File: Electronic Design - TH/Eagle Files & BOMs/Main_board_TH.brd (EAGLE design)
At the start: 98 x 137 mm, 43 parts, among them M1 ARDUINO-NANO-3.0, Q1 IRF9520, Q2 IRF9520

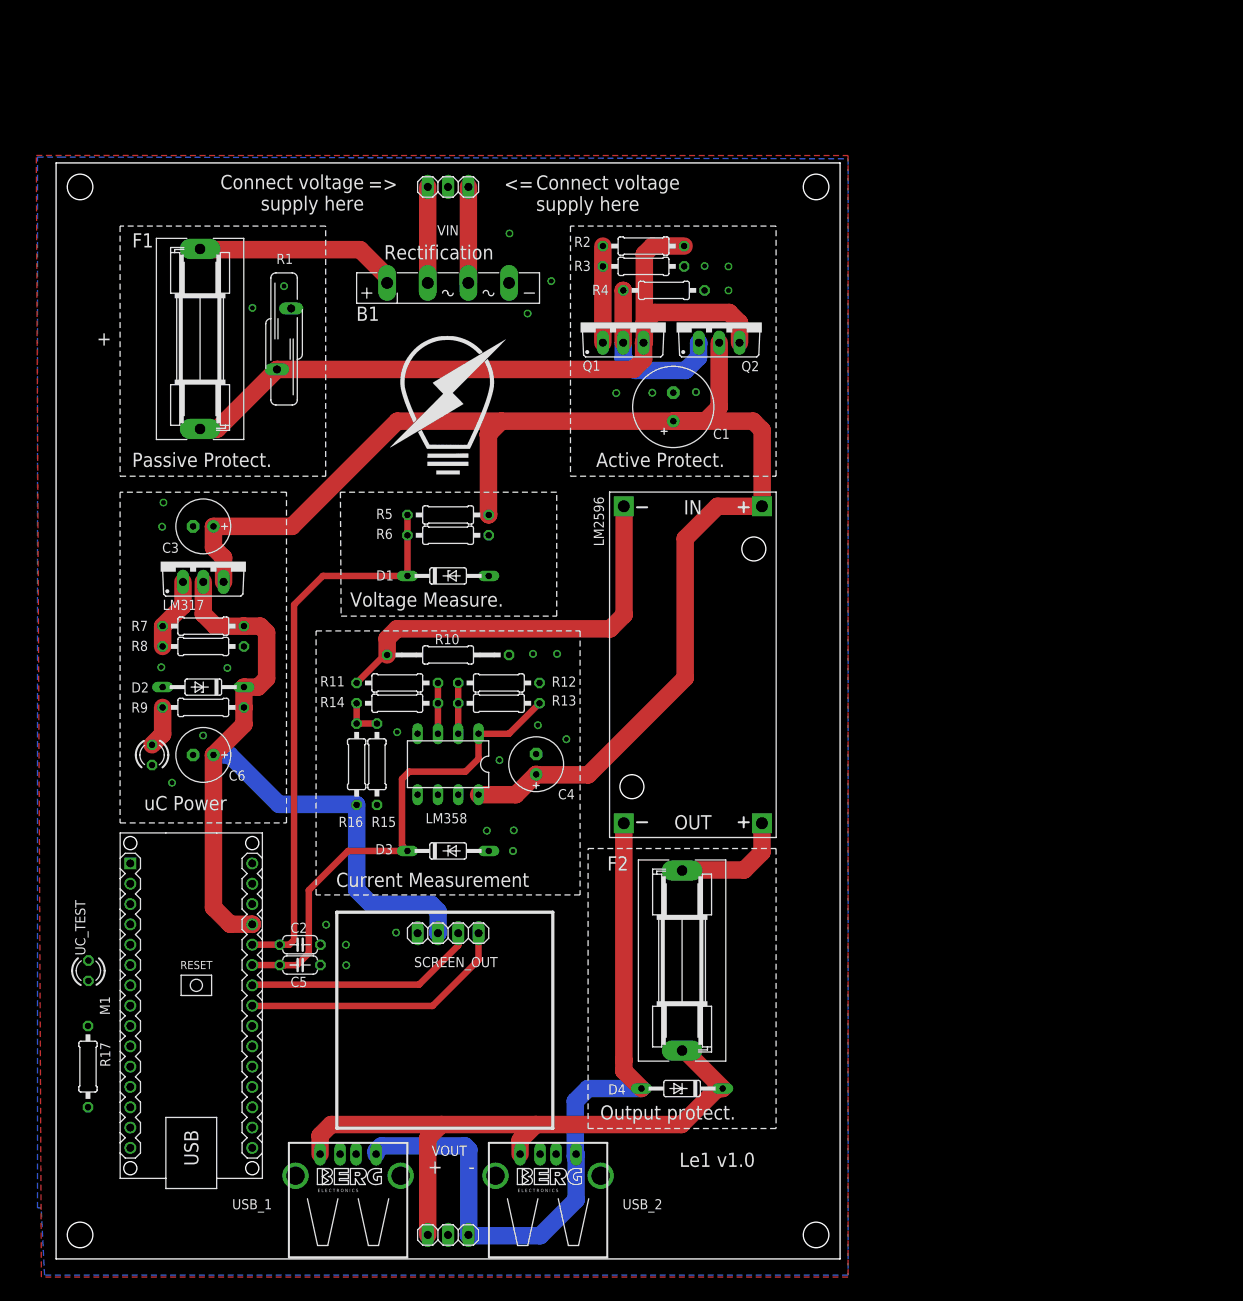
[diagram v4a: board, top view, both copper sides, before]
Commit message: adding in test points and jumpers
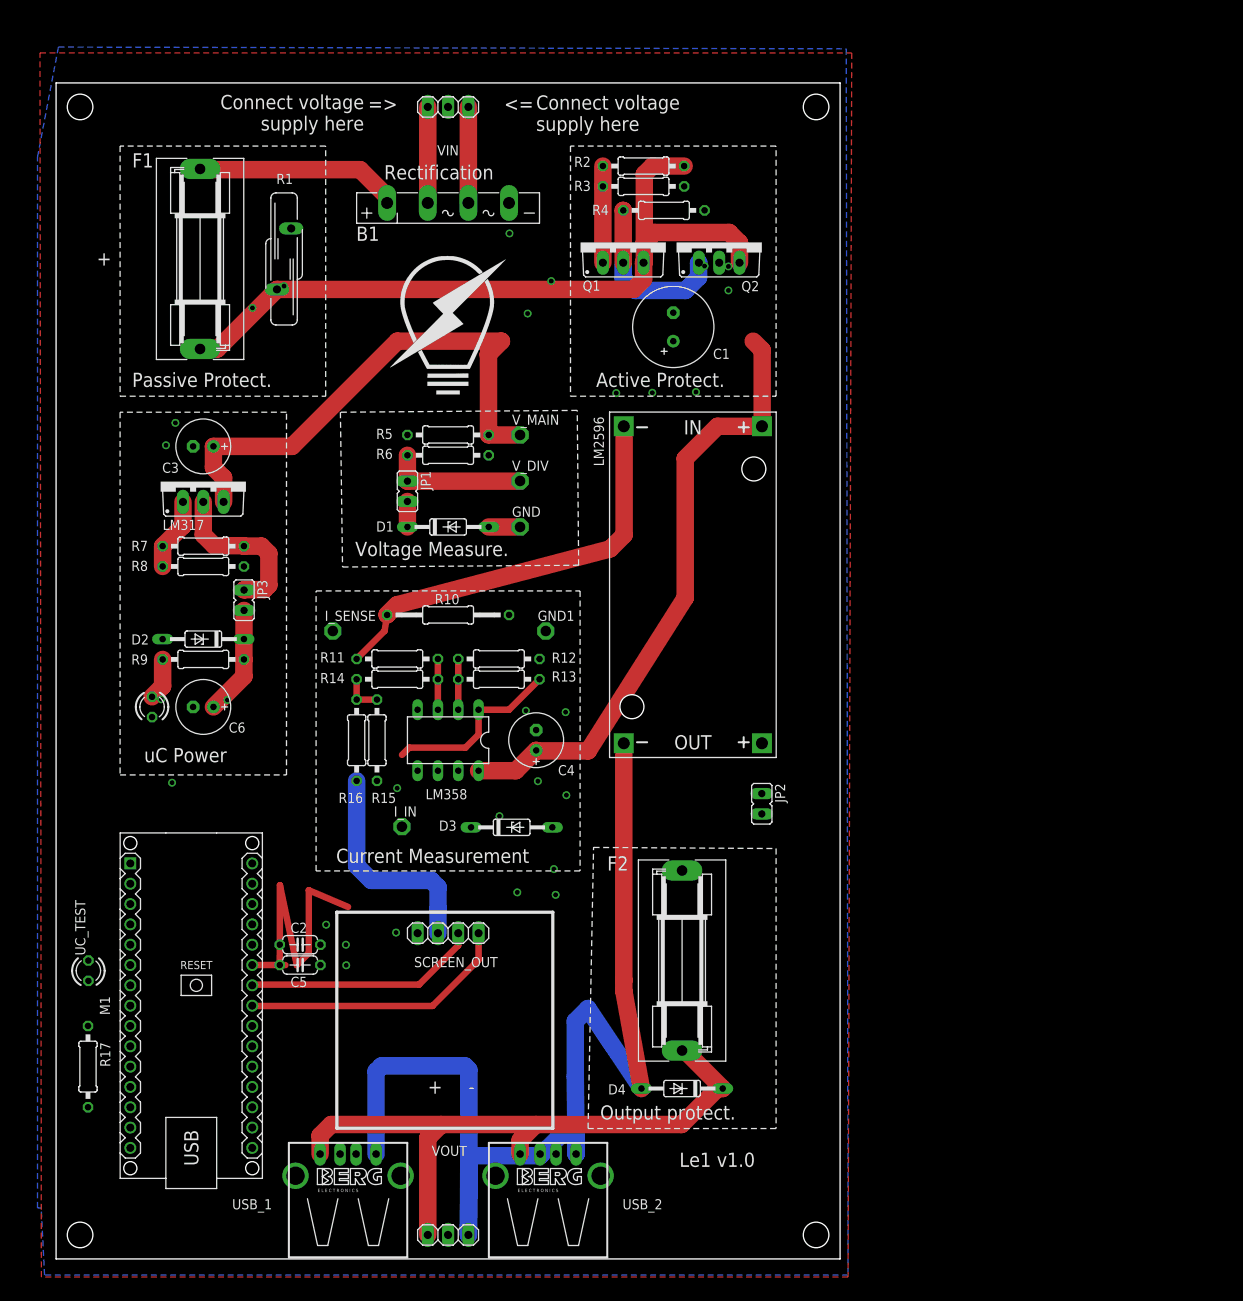
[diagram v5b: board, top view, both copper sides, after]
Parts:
- added GND, GND1, I_IN, I_SENSE, V_DIV, V_MAIN: TPPAD1-13, testpad:P1-13
- added JP1, JP2, JP3: (no value), jumper:JP1
- moved R2 10.0 mm to (73.4, 136.6)
- moved B1 10.0 mm to (49.0, 132.0)
- moved C1 10.0 mm to (77.2, 116.5)
- moved C3 10.0 mm to (18.4, 101.6)
- moved F1 10.0 mm to (18.0, 125.0)
- moved LM2596 10.0 mm to (79.6, 84.3)
- moved LM317 10.0 mm to (18.4, 97.2)
- moved Q1 10.0 mm to (70.9, 127.1)
- moved Q2 10.0 mm to (82.9, 127.1)
- moved R1 10.0 mm to (28.5, 125.0)
- moved R3 10.0 mm to (73.4, 134.1)
- moved R4 10.0 mm to (76.0, 131.1)
- moved R5 10.0 mm to (49.0, 103.0)
- moved R6 10.0 mm to (49.0, 100.5)
- moved R7 10.0 mm to (18.4, 89.1)
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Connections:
- removed net VOUT_PREFUSE: F2.1, LM2596.OUT+
- new net N$15: JP2.1, LM2596.OUT+
- new net N$16: F2.1, JP2.2
- new net N$17: JP1.1, R5.1, R6.2, V_DIV.TP
- new net N$18: JP3.1, LM317.2, R7.2
- net +5V: now also JP3.2; no longer LM317.2, R7.2
- net GND: now also GND.TP, GND1.TP
- net I_IN: now also I_IN.TP
- net N$4: now also I_SENSE.TP
- net VIN_PROTECTED: now also V_MAIN.TP
- net V_IN: now also JP1.2; no longer R5.1, R6.2
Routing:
- net V_IN: track 70.7 -> 3.18 mm
- net +5V: track 101.9 -> 41.3 mm
- net N$10: track 94.4 -> 146.7 mm
- net VIN_PROTECTED: track 179.1 -> 142.5 mm
- net N$18: track 0.00 -> 20.6 mm
- net N$17: track 0.00 -> 17.3 mm
- net VOUT_PREFUSE: track 16.9 -> 0.00 mm
- net GND: track 0.00 -> 3.92 mm, vias 30 -> 29
- net N$4: track 51.7 -> 52.4 mm
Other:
- board size 98 x 137 mm -> 98 x 147 mm

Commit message: putting all components into the right places before rounting
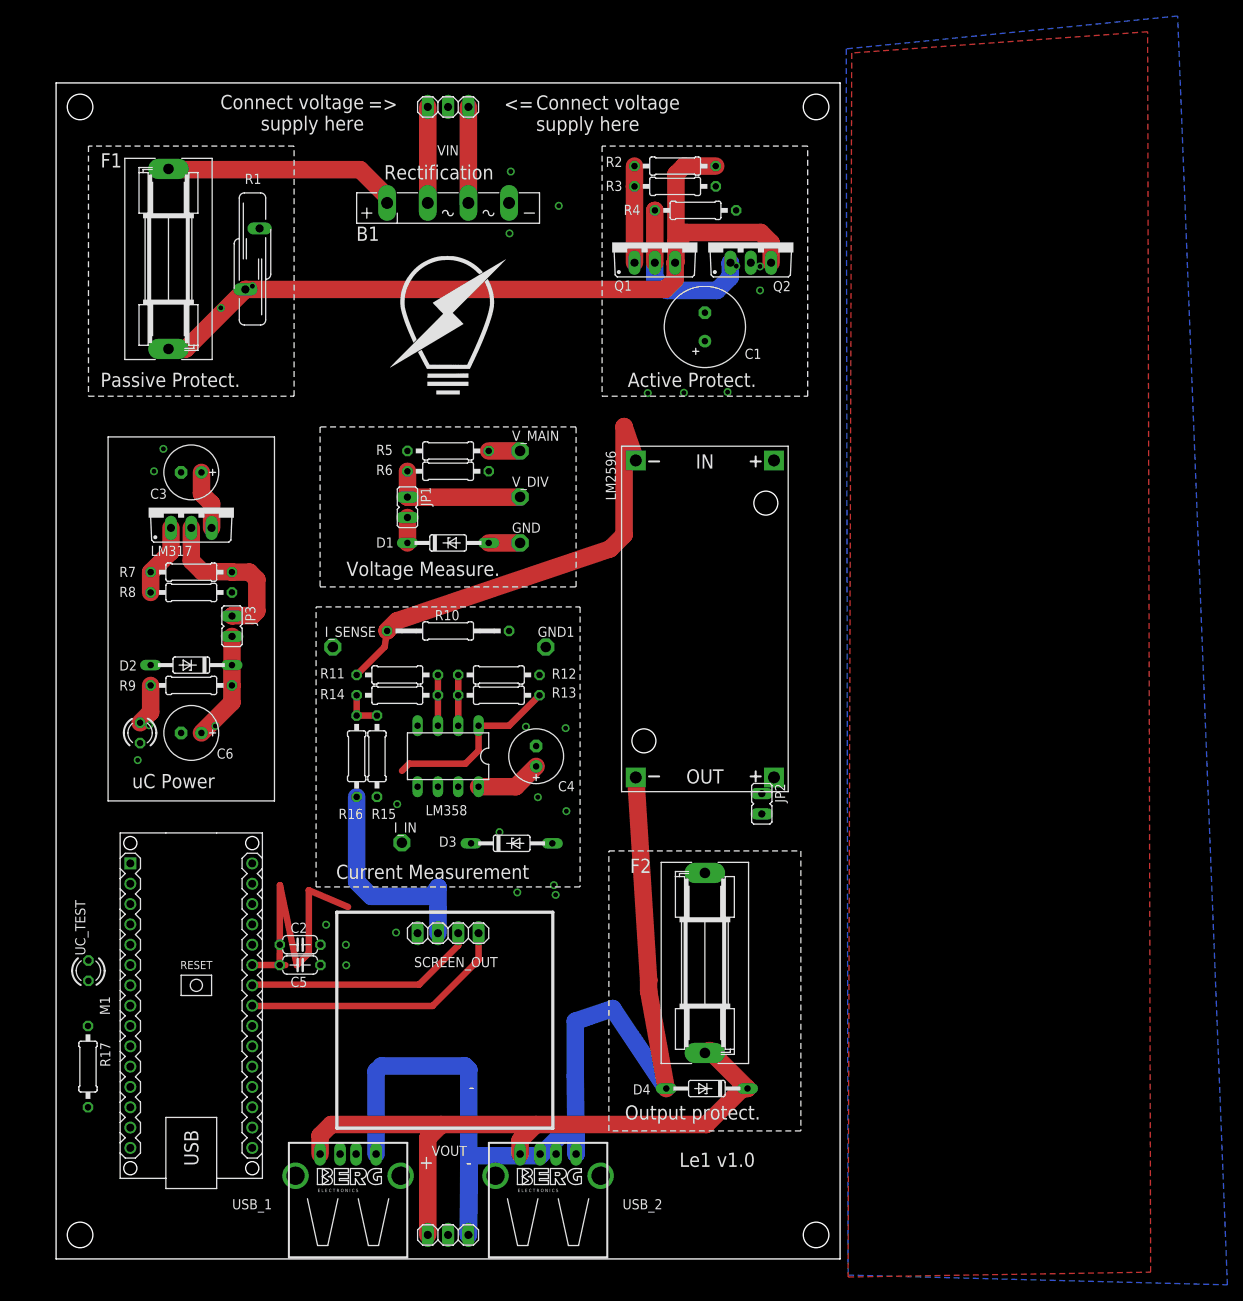
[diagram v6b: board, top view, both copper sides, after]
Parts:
- moved LM2596 4.53 mm to (81.1, 80.0)
- moved Q1 3.95 mm to (74.8, 127.1)
- moved Q2 3.95 mm to (86.8, 127.1)
- moved R4 3.95 mm to (79.9, 131.1)
- moved F1 3.95 mm to (14.1, 125.0)
- moved R1 3.95 mm to (24.6, 125.0)
- moved C1 3.95 mm to (81.1, 116.5)
- moved R2 3.95 mm to (77.4, 136.6)
- moved R3 3.95 mm to (77.4, 134.1)
- moved C3 3.58 mm to (16.9, 98.3)
- moved C6 3.58 mm to (16.9, 65.8)
- moved D2 3.58 mm to (16.9, 74.2)
- moved JP3 3.58 mm to (22.0, 79.1)
- moved LM317 3.58 mm to (16.9, 93.9)
- moved R7 3.58 mm to (16.9, 85.8)
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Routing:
- net VIN_PROTECTED: track 142.5 -> 19.6 mm
- net VIN_UNPROTECTED: track 93.1 -> 101.0 mm
- net N$4: track 52.4 -> 57.4 mm
- net N$1: track 26.4 -> 30.3 mm
- net VOUT_FINAL: track 81.1 -> 84.6 mm
- net N$10: track 146.7 -> 145.2 mm

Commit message: adding another jumper after current sensing and more routing done
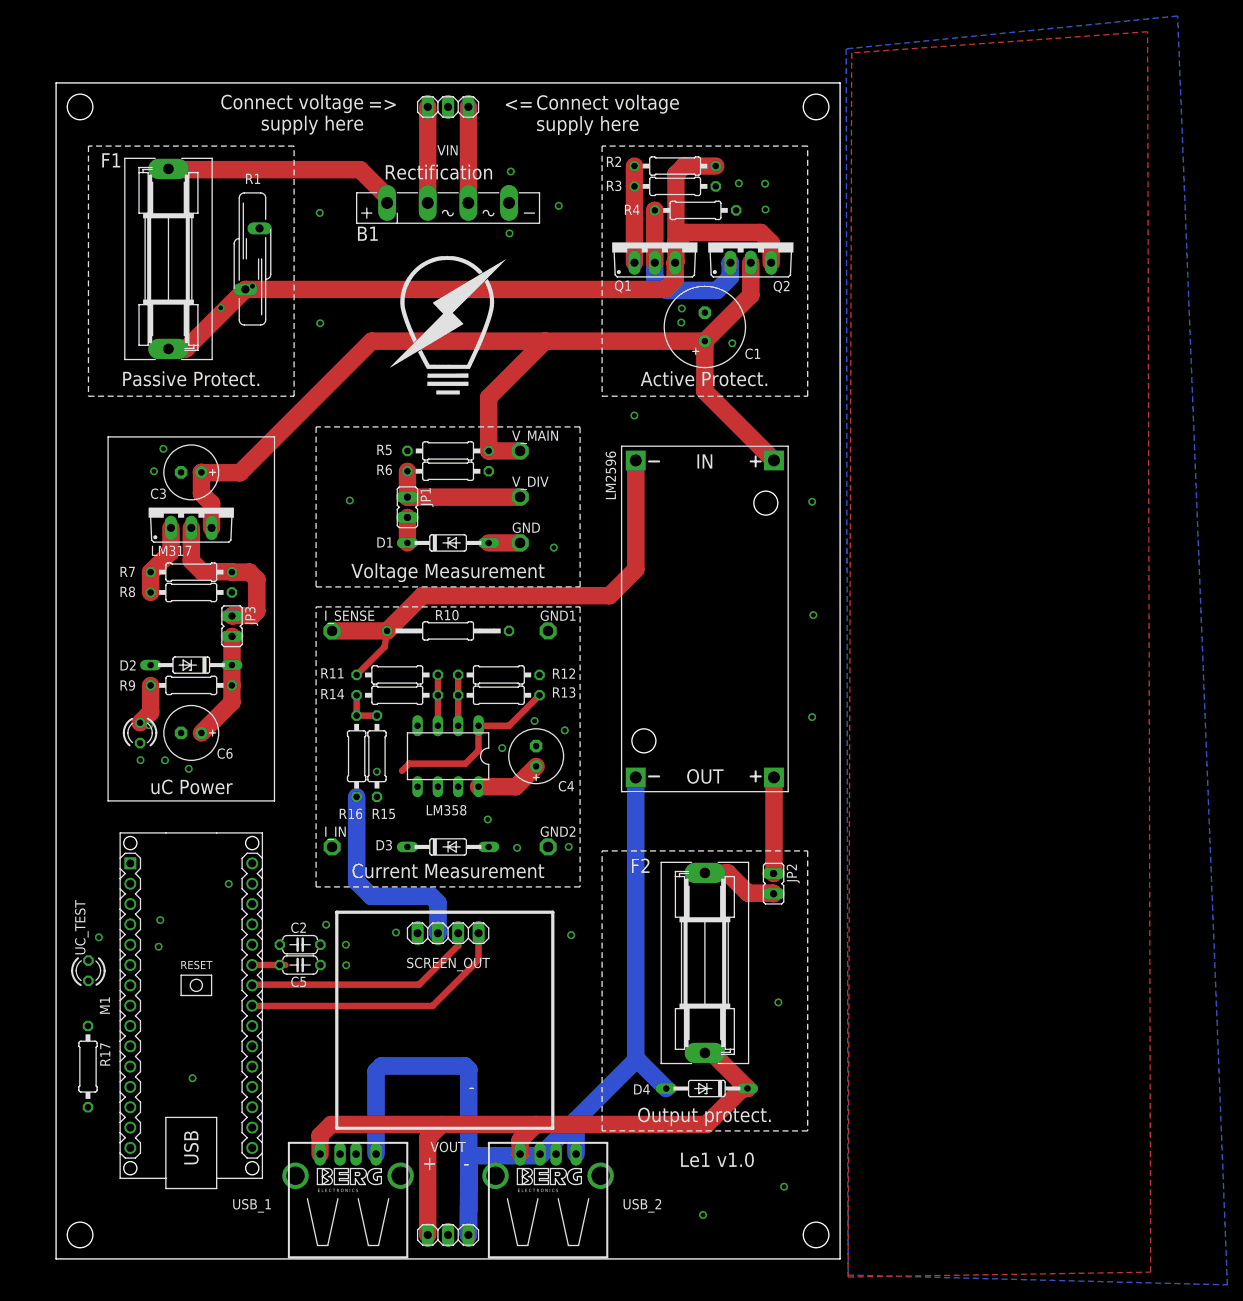
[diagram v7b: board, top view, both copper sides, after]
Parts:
- added GND2: TPPAD1-13, testpad:P1-13
- moved JP2 10.1 mm to (89.7, 46.9)
- moved I_IN 8.75 mm to (34.5, 51.5)
- moved D3 7.96 mm to (49.0, 51.5)
- moved GND1 2.03 mm to (61.5, 78.5)
- moved I_SENSE 2.01 mm to (34.5, 78.5)
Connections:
- net GND: now also GND2.TP
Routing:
- net VIN_PROTECTED: track 19.6 -> 136.7 mm
- net I_IN: track 62.6 -> 27.1 mm
- net N$10: track 145.2 -> 123.7 mm
- net N$15: track 0.00 -> 12.0 mm
- net N$16: track 0.00 -> 9.67 mm
- net N$4: track 57.4 -> 61.8 mm
- net +5V: track 41.5 -> 39.3 mm
- net GND: vias 29 -> 45
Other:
- board text added: "IN"
- board text added: "OUT"
- board text added: "Voltage Measurement"
- board text removed: "Voltage Measure."

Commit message: finishing routing
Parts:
- added JP4: (no value), jumper:JP1
- moved GND1 0.50 mm to (61.0, 78.5)
- moved GND2 0.50 mm to (61.0, 51.5)
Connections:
- removed net GND.1: M1.J1.4
- new net I_IN_PRE: I_IN.TP, JP4.2, LM358.1, R13.1
- net GND: now also M1.J1.4
- net I_IN: now also JP4.1; no longer I_IN.TP, LM358.1, R13.1
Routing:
- net V_IN: track 3.18 -> 71.0 mm
- net VIN_PROTECTED: track 136.7 -> 195.1 mm
- net I_IN_PRE: track 0.00 -> 53.3 mm
- net +5V: track 39.3 -> 90.3 mm
- net I_IN: track 27.1 -> 45.9 mm
- net N$10: track 123.7 -> 117.8 mm
- net N$14: track 0.00 -> 5.66 mm
- net N$13: track 0.00 -> 5.29 mm
- net N$17: track 17.3 -> 19.9 mm
- net GND: vias 45 -> 44
